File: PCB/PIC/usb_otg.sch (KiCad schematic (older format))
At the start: 15 parts, among them J6 ZX62-AB-5PA, P3 CONN_6, U10 MIC2025-2YM, U15 TPS2051B, U9 PRTR5V0U2X

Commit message: Correcciones al esquematico segun rev01
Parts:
- removed P3: CONN_6, symbol CONN_6
- added P3: CONN_5, symbol CONN_5
- C32, C33, C64, C65: symbol C -> C-RESCUE-ciaa-pic
- R48, R49: symbol R -> R-RESCUE-ciaa-pic
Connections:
- net D+: now also P3.3
- net D-: now also P3.2
- net GND: now also P3.4
- net GND_SH: now also P3.5
- net at C65.1, U15.1 (OUT): now also P3.1
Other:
- note added: "El conector USB en paralelo con otro, \nno creo sea buena práctica. Además el \nruteo del USB debe ser prolijo y limpio."
- note added: "GND_SH debería ser un símbolo de tierra. Hay varios en KiCAD."
- moved on the sheet: C31, C32, C33, C64, C65, FB1, FB15, J6, R48, R49, TR2, U10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

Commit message: elimino conector salida reles
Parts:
- C31, C32, C33, C64, C65: footprint ~ -> Capacitors_SMD:C_0603
- FB1, FB15, U9: footprint ~ -> (none)
- R48, R49: footprint ~ -> Resistors_SMD:R_0603
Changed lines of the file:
@@
 encoding utf-8
 Sheet 4 13
-Title "CIAA-Microchip"
+Title "USB"
 Date "16 feb 2016"
 Rev "1.0"
@@
 F 0 "U10" H 2900 5900 60  0000 L CNN
 F 1 "MIC2025-2YM" H 2650 4700 60  0000 L CNN
-F 2 "" H 2950 5300 60  0000 C CNN
+F 2 "" H 2950 5300 60  0001 C CNN
 F 3 "" H 2950 5300 60  0000 C CNN
 	1    2950 5300
@@
 F 0 "U9" H 5850 5550 70  0000 C CNN
 F 1 "PRTR5V0U2X" H 5850 4900 70  0000 C CNN
-F 2 "~" H 7400 4600 60  0000 C CNN
+F 2 "" H 7400 4600 60  0001 C CNN
 F 3 "~" H 7400 4600 60  0000 C CNN
 	1    5850 5250
@@
 F 0 "C31" H 7300 5350 40  0000 L CNN
 F 1 "10uF" H 7300 5150 40  0000 L CNN
-F 2 "~" H 7350 5100 30  0000 C CNN
+F 2 "Capacitors_SMD:C_0603" H 7350 5100 30  0001 C CNN
 F 3 "~" H 7250 5250 300 0000 C CNN
 	1    7250 5250
@@
 F 0 "C32" H 7600 5350 40  0000 L CNN
 F 1 "100nF" H 7606 5165 40  0000 L CNN
-F 2 "~" H 7638 5100 30  0000 C CNN
+F 2 "Capacitors_SMD:C_0603" H 7638 5100 30  0001 C CNN
 F 3 "~" H 7600 5250 60  0000 C CNN
 	1    7600 5250
@@
 F 0 "J6" V 10500 4300 60  0000 C CNN
 F 1 "ZX62-AB-5PA" V 10600 4300 60  0000 C CNN
-F 2 "" H 10550 4300 60  0000 C CNN
+F 2 "" H 10550 4300 60  0001 C CNN
 F 3 "" H 10550 4300 60  0000 C CNN
 	1    10550 4300
@@
 F 0 "C33" H 4000 5600 40  0000 L CNN
 F 1 "100nF" H 4006 5415 40  0000 L CNN
-F 2 "~" H 4038 5350 30  0000 C CNN
+F 2 "Capacitors_SMD:C_0603" H 4038 5350 30  0001 C CNN
 F 3 "~" H 4000 5500 60  0000 C CNN
 	1    4000 5500
@@
 F 0 "FB1" H 10100 5500 60  0000 C CNN
 F 1 "MMZ1608B601C" H 10100 5250 60  0000 C CNN
-F 2 "~" H 10100 5350 60  0000 C CNN
+F 2 "" H 10100 5350 60  0001 C CNN
 F 3 "~" H 10100 5350 60  0000 C CNN
 	1    10100 5350
@@
 F 0 "R49" V 1580 5200 40  0000 C CNN
 F 1 "10k" V 1507 5201 40  0000 C CNN
-F 2 "~" V 1430 5200 30  0000 C CNN
+F 2 "Resistors_SMD:R_0603" V 1430 5200 30  0001 C CNN
 F 3 "~" H 1500 5200 30  0000 C CNN
 	1    1500 5200
@@
 F 0 "R48" V 1580 5000 40  0000 C CNN
 F 1 "10k" V 1507 5001 40  0000 C CNN
-F 2 "~" V 1430 5000 30  0000 C CNN
+F 2 "Resistors_SMD:R_0603" V 1430 5000 30  0001 C CNN
 F 3 "~" H 1500 5000 30  0000 C CNN
 	1    1500 5000
@@
 F 0 "FB15" H 8250 3800 60  0000 C CNN
 F 1 "BLM18KG221SN1" H 8250 3700 60  0000 C CNN
-F 2 "~" H 8250 3900 60  0000 C CNN
+F 2 "" H 8250 3900 60  0001 C CNN
 F 3 "~" H 8250 3900 60  0000 C CNN
 	1    8250 3900
@@
 F 0 "TR2" V 8650 4700 60  0000 C CNN
 F 1 "DLW21HN900SQ2" V 8550 4700 60  0000 C CNN
-F 2 "" H 8250 4700 60  0000 C CNN
+F 2 "" H 8250 4700 60  0001 C CNN
 F 3 "" H 8250 4700 60  0000 C CNN
 	1    8250 4700
@@
 F 0 "U15" H 4700 1050 60  0000 C CNN
 F 1 "TPS2051B" H 4450 2100 60  0000 C CNN
-F 2 "" H 4700 1050 60  0000 C CNN
+F 2 "" H 4700 1050 60  0001 C CNN
 F 3 "" H 4700 1050 60  0000 C CNN
 	1    4500 1700
@@
 F 0 "C65" H 6100 1950 40  0000 L CNN
 F 1 "100nF" H 6106 1765 40  0000 L CNN
-F 2 "~" H 6138 1700 30  0000 C CNN
+F 2 "Capacitors_SMD:C_0603" H 6138 1700 30  0001 C CNN
 F 3 "~" H 6100 1850 60  0000 C CNN
 	1    6100 1850
@@
 F 0 "C64" H 3150 1850 40  0000 L CNN
 F 1 "100nF" H 3156 1665 40  0000 L CNN
-F 2 "~" H 3188 1600 30  0000 C CNN
+F 2 "Capacitors_SMD:C_0603" H 3188 1600 30  0001 C CNN
 F 3 "~" H 3150 1750 60  0000 C CNN
 	1    3150 1750
@@
 F 0 "P3" V 8450 1650 50  0000 C CNN
 F 1 "CONN_5" V 8550 1650 50  0000 C CNN
-F 2 "" H 8500 1650 60  0000 C CNN
+F 2 "" H 8500 1650 60  0001 C CNN
 F 3 "" H 8500 1650 60  0000 C CNN
 	1    8500 1650

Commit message: rev02 aignacion footprint
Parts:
- J6: footprint (none) -> footprints:USB_microAB_ZX62-AB&B-5PA-11
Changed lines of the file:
@@
 F 0 "J6" V 10500 4300 60  0000 C CNN
 F 1 "ZX62-AB-5PA" V 10600 4300 60  0000 C CNN
-F 2 "" H 10550 4300 60  0001 C CNN
+F 2 "footprints:USB_microAB_ZX62-AB&B-5PA-11" H 10550 4300 60  0001 C CNN
 F 3 "" H 10550 4300 60  0000 C CNN
 	1    10550 4300

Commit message: rev02 se completa campo num. de frabicante(manf#) CIAA-PIC
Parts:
- C32, C33, C64, C65: manf# (none) -> C0603C104K5RACTU
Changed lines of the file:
@@
 F 2 "Capacitors_SMD:C_0603" H 7638 5100 30  0001 C CNN
 F 3 "~" H 7600 5250 60  0000 C CNN
+F 4 "C0603C104K5RACTU" H 7600 5250 60  0001 C CNN "manf#"
 	1    7600 5250
 	1    0    0    -1
@@
 F 2 "Capacitors_SMD:C_0603" H 4038 5350 30  0001 C CNN
 F 3 "~" H 4000 5500 60  0000 C CNN
+F 4 "C0603C104K5RACTU" H 4000 5500 60  0001 C CNN "manf#"
 	1    4000 5500
 	1    0    0    -1
@@
 F 2 "Capacitors_SMD:C_0603" H 6138 1700 30  0001 C CNN
 F 3 "~" H 6100 1850 60  0000 C CNN
+F 4 "C0603C104K5RACTU" H 6100 1850 60  0001 C CNN "manf#"
 	1    6100 1850
 	1    0    0    -1
@@
 F 2 "Capacitors_SMD:C_0603" H 3188 1600 30  0001 C CNN
 F 3 "~" H 3150 1750 60  0000 C CNN
+F 4 "C0603C104K5RACTU" H 3150 1750 60  0001 C CNN "manf#"
 	1    3150 1750
 	1    0    0    -1

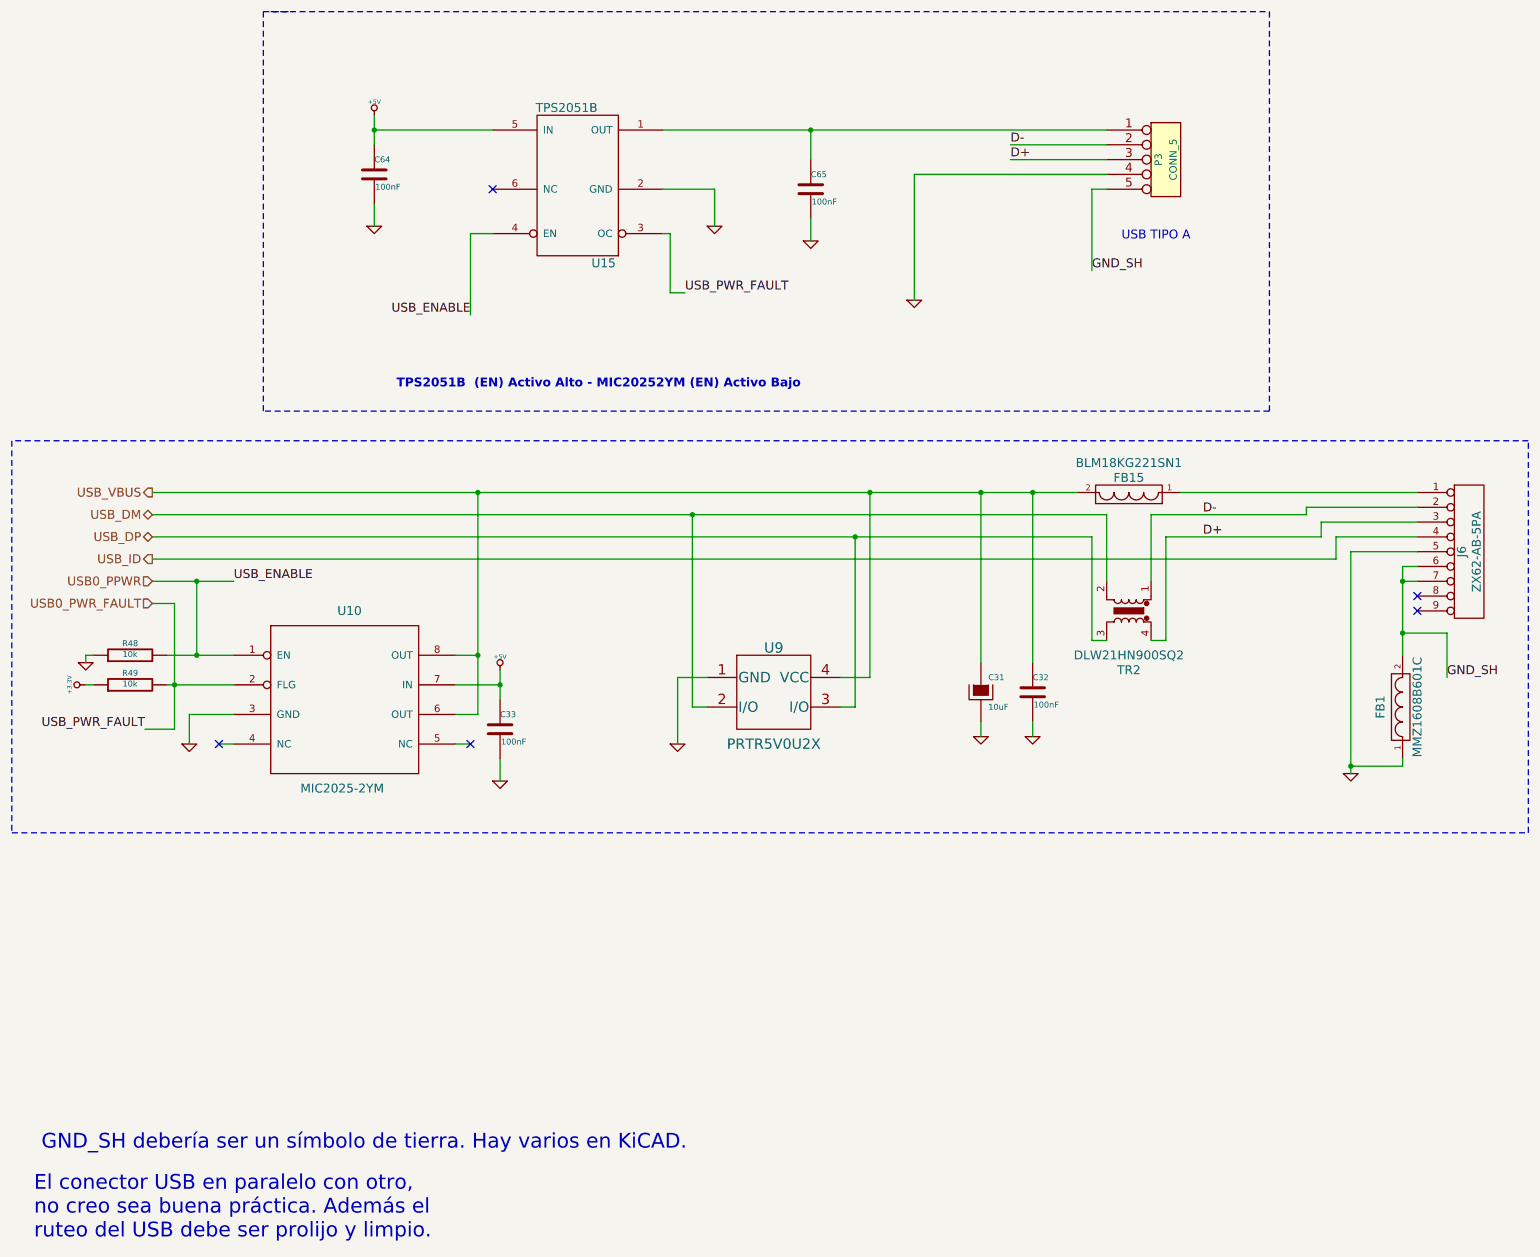
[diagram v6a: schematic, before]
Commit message: se completa campo num. de frabicante(manf#) CIAA-PIC
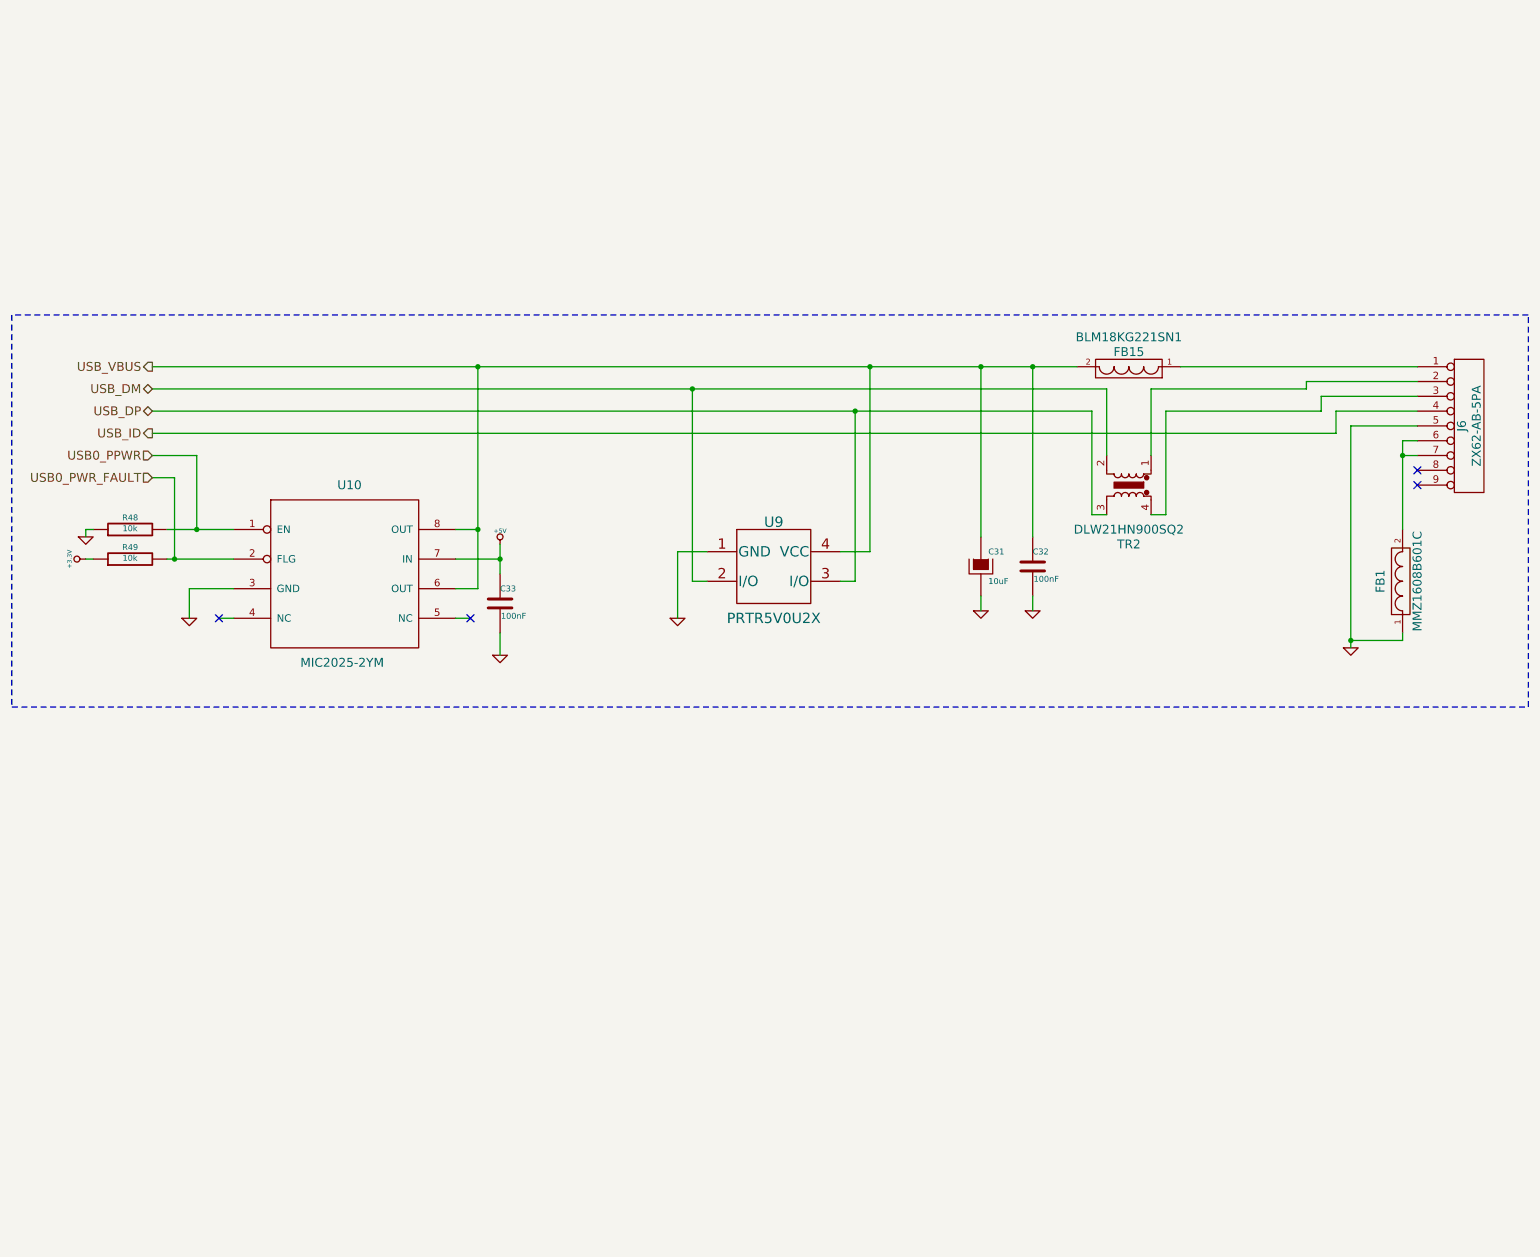
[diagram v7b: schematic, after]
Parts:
- removed C64, C65: 100nF, Capacitors_SMD:C_0603, symbol C-RESCUE-ciaa-pic
- removed P3: CONN_5, symbol CONN_5
- removed U15: TPS2051B, symbol TPS2051B
- C31: footprint Capacitors_SMD:C_0603 -> footprints:c_1206_tantalio; manf# (none) -> T491A106K006AT7280
- FB1: footprint (none) -> footprints:SM0603; manf# (none) -> MMZ1608B601CTAH0
- FB15: footprint (none) -> footprints:SM0603; manf# (none) -> BLM18KG221SN1D
- J6: manf# (none) -> ZX62-AB-5PA(11)
- TR2: footprint (none) -> footprints:SRF2012; manf# (none) -> SRF2012-900Y
- U10: footprint (none) -> footprints:-SOIC8; manf# (none) -> MIC2025-2YM
- U9: footprint (none) -> footprints:sot143B; manf# (none) -> PRTR5V0U2X,215
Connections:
- net D+: no longer names the net of J6.3 (P3), TR2.4
- net D-: no longer names the net of J6.2 (P2), TR2.1
- net GND_SH: no longer names the net of FB1.2, J6.6 (P6), J6.7 (P7)
- no-connect marks 5 -> 4
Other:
- note removed: "El conector USB en paralelo con otro, \nno creo sea buena práctica. Además el \nruteo del USB debe ser prolijo y limpio."
- note removed: "GND_SH debería ser un símbolo de tierra. Hay varios en KiCAD."
- note removed: "TPS2051B (EN) Activo Alto - MIC20252YM (EN) Activo Bajo"
- note removed: "USB TIPO A"
- moved on the sheet: C31, C32, C33, FB1, FB15, J6, R48, R49, TR2, U10, U9

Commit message: BOM File CIAA-PIC
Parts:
- R48, R49: manf# (none) -> RC0603JR-0710KL
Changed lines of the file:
@@
 F 2 "Resistors_SMD:R_0603" V 1430 4350 30  0001 C CNN
 F 3 "~" H 1500 4350 30  0000 C CNN
+F 4 "RC0603JR-0710KL" V 1500 4350 60  0001 C CNN "manf#"
 	1    1500 4350
 	0    -1   -1   0
@@
 F 2 "Resistors_SMD:R_0603" V 1430 4150 30  0001 C CNN
 F 3 "~" H 1500 4150 30  0000 C CNN
+F 4 "RC0603JR-0710KL" V 1500 4150 60  0001 C CNN "manf#"
 	1    1500 4150
 	0    -1   -1   0
